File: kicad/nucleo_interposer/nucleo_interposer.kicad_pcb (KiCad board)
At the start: 2 copper layers, 20.3 x 52.3 mm, 5 parts, among them J1 Conn_02x08_Odd_Even, U1 NUCLEO-F303K8-HEADER

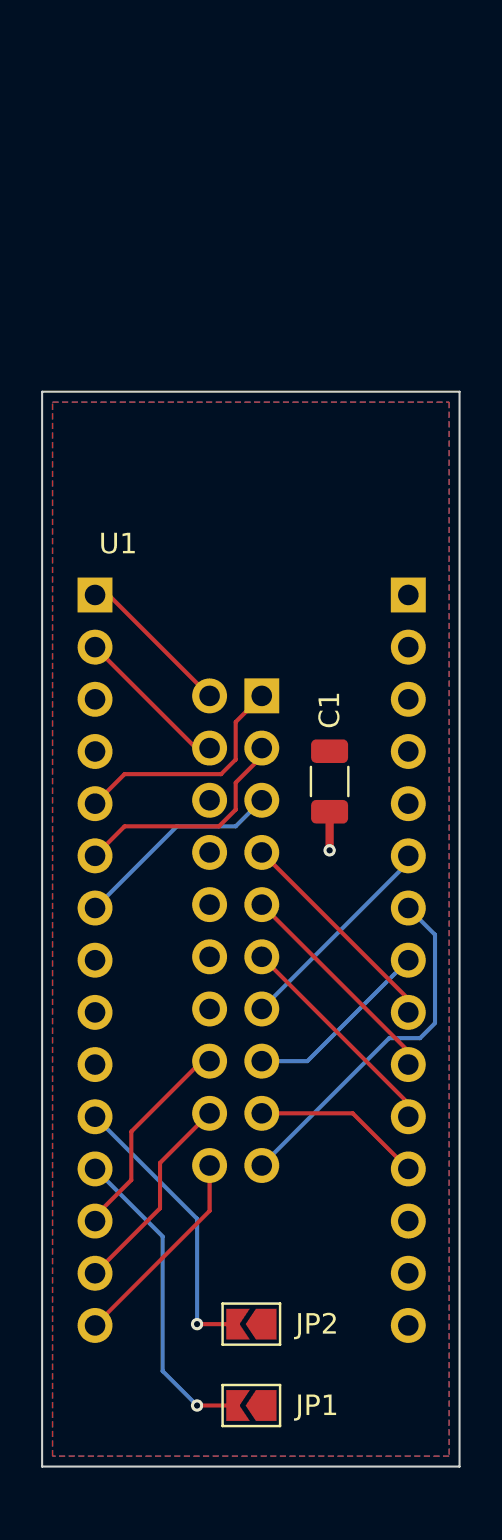
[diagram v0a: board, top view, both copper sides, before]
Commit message: add nucleo interposer step and make it smaller
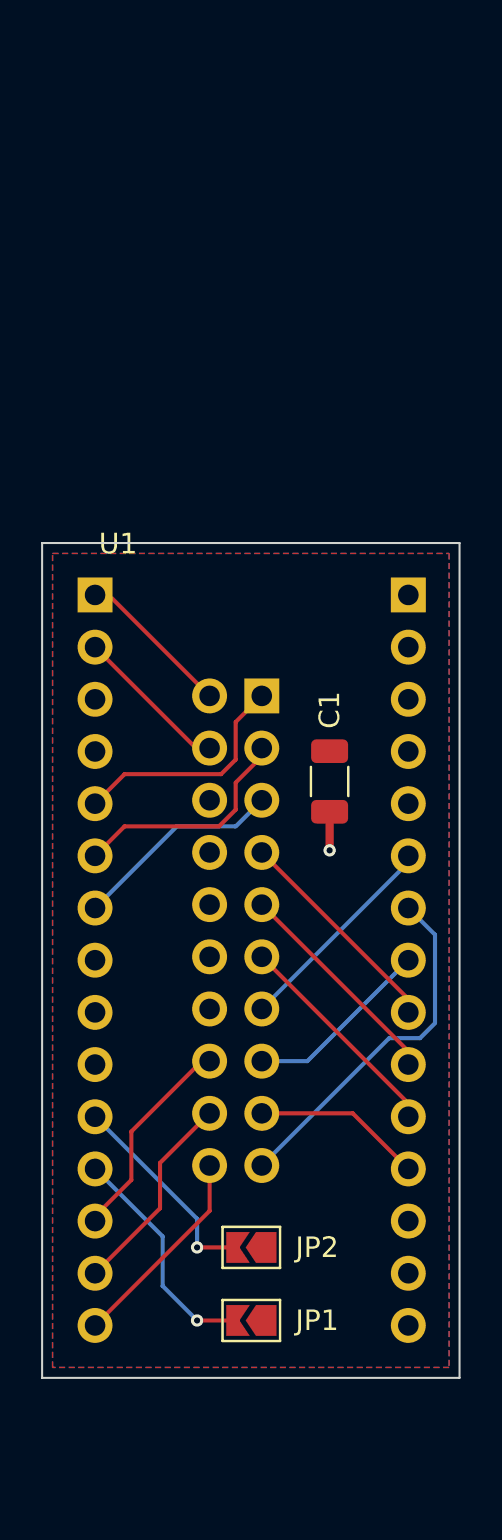
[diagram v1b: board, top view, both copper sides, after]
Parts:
- moved JP1 4.14 mm to (143.9, 106.3)
- moved JP2 3.73 mm to (143.9, 102.7)
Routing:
- net Net-(U1-PA8): track 15.5 -> 11.4 mm
- net Net-(U1-PF1): track 14.1 -> 10.3 mm
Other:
- board size 20.3 x 52.3 mm -> 20.3 x 40.6 mm
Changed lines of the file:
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@@
     )
     (pad_to_mask_clearance 0)
-    (grid_origin 144.4244 75.8952)
+    (grid_origin 133.731 113.411)
     (pcbplotparams
       (layerselection 0x00010fc_ffffffff)
@@
   (net 30 "unconnected-(U1-PB3)")
   (footprint "Jumper:SolderJumper-2_P1.3mm_Open_TrianglePad1.0x1.5mm" (layer "F.Cu")
-    (at 143.9164 110.4392 180)
+    (at 143.9164 106.299 180)
     (descr "SMD Solder Jumper, 1x1.5mm Triangular Pads, 0.3mm gap, open")
     (tags "solder jumper open")
@@
   )
   (footprint "Jumper:SolderJumper-2_P1.3mm_Open_TrianglePad1.0x1.5mm" (layer "F.Cu")
-    (at 143.9164 106.4768 180)
+    (at 143.9164 102.743 180)
     (descr "SMD Solder Jumper, 1x1.5mm Triangular Pads, 0.3mm gap, open")
     (tags "solder jumper open")
@@
     )
   )
-  (gr_rect (start 133.731 61.087) (end 154.051 113.411)
+  (gr_rect (start 133.731 68.453) (end 154.051 109.093)
     (stroke (width 0.1) (type default)) (fill none) (layer "Edge.Cuts"))
   (segment (start 147.7264 81.5358) (end 147.7264 83.4136) (width 0.4) (layer "F.Cu") (net 1))
@@
   (segment (start 141.8844 100.9646) (end 141.8844 98.7552) (width 0.2) (layer "F.Cu") (net 18))
   (segment (start 136.308 106.541) (end 141.8844 100.9646) (width 0.2) (layer "F.Cu") (net 18))
-  (segment (start 143.1914 110.4392) (end 141.2748 110.4392) (width 0.2) (layer "F.Cu") (net 19))
-  (via (at 141.2748 110.4392) (size 0.6) (drill 0.3) (layers "F.Cu" "B.Cu") (net 19))
+  (segment (start 143.1914 106.299) (end 141.2748 106.299) (width 0.2) (layer "F.Cu") (net 19))
+  (via (at 141.2748 106.299) (size 0.6) (drill 0.3) (layers "F.Cu" "B.Cu") (net 19))
   (segment (start 139.5984 102.2114) (end 136.308 98.921) (width 0.2) (layer "B.Cu") (net 19))
-  (segment (start 139.5984 108.7628) (end 139.5984 102.2114) (width 0.2) (layer "B.Cu") (net 19))
-  (segment (start 141.2748 110.4392) (end 139.5984 108.7628) (width 0.2) (layer "B.Cu") (net 19))
-  (segment (start 143.1914 106.4768) (end 141.2748 106.4768) (width 0.2) (layer "F.Cu") (net 20))
-  (via (at 141.2748 106.4768) (size 0.6) (drill 0.3) (layers "F.Cu" "B.Cu") (net 20))
+  (segment (start 141.2748 106.299) (end 139.5984 104.6226) (width 0.2) (layer "B.Cu") (net 19))
+  (segment (start 139.5984 104.6226) (end 139.5984 102.2114) (width 0.2) (layer "B.Cu") (net 19))
+  (segment (start 143.1914 102.743) (end 141.2748 102.743) (width 0.2) (layer "F.Cu") (net 20))
+  (via (at 141.2748 102.743) (size 0.6) (drill 0.3) (layers "F.Cu" "B.Cu") (net 20))
   (segment (start 141.2748 101.3478) (end 136.308 96.381) (width 0.2) (layer "B.Cu") (net 20))
-  (segment (start 141.2748 106.4768) (end 141.2748 101.3478) (width 0.2) (layer "B.Cu") (net 20))
+  (segment (start 141.2748 101.3478) (end 141.2748 102.743) (width 0.2) (layer "B.Cu") (net 20))
   (zone (net 2) (net_name "+5V") (layer "F.Cu") (hatch edge 0.508)
     (connect_pads (clearance 0.254))
@@
     (polygon
       (pts
-        (xy 153.543 112.903)
-        (xy 134.239 112.903)
-        (xy 134.239 61.595)
-        (xy 153.543 61.595)
+        (xy 153.543 108.585)
+        (xy 134.239 108.585)
+        (xy 134.239 68.961)
+        (xy 153.543 68.961)
       )
     )
@@
     (polygon
       (pts
-        (xy 153.543 112.903)
-        (xy 134.239 112.903)
-        (xy 134.239 61.595)
-        (xy 153.543 61.595)
+        (xy 153.543 108.585)
+        (xy 134.239 108.585)
+        (xy 134.239 68.961)
+        (xy 153.543 68.961)
       )
     )

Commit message: move JPS and cap to back
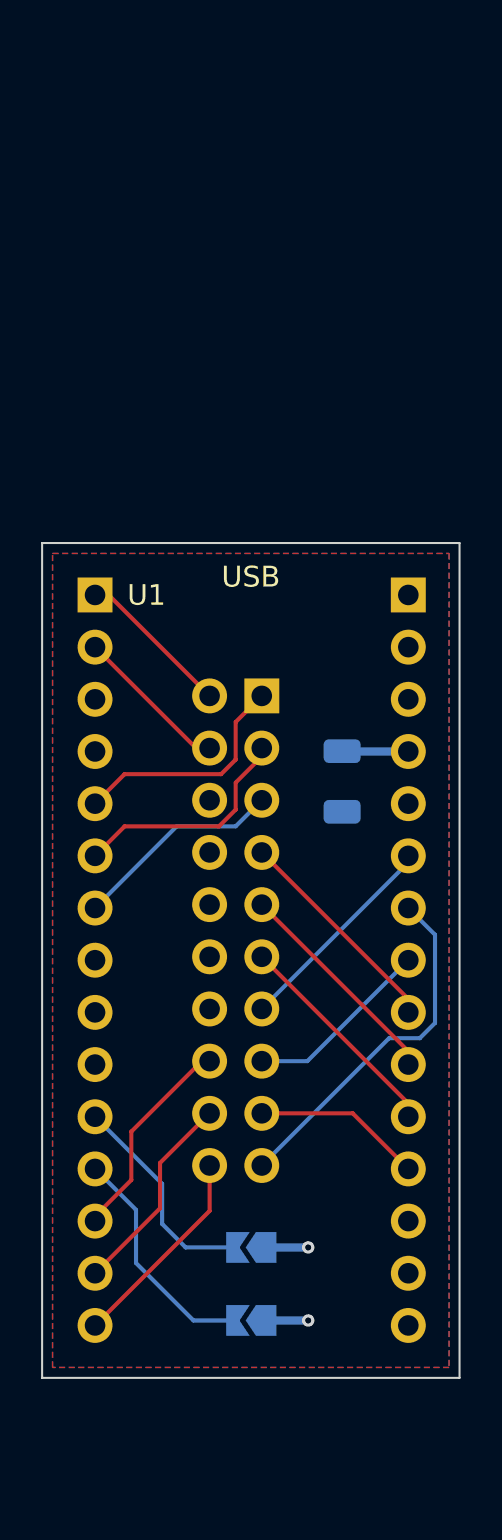
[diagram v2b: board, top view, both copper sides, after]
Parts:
- C1, JP1, JP2: moved to B.Cu
- moved C1 0.61 mm to (148.3, 80.1)
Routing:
- net +5V: track 0.00 -> 7.34 mm, vias 0 -> 2
- net GND: track 1.88 -> 0.00 mm, vias 1 -> 0
- net Net-(U1-PF1): track 10.3 -> 10.7 mm, vias 1 -> 0
- net Net-(U1-PA8): track 11.4 -> 11.5 mm, vias 1 -> 0
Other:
- board text added: "USB"

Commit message: add mounts for nucleo interposer
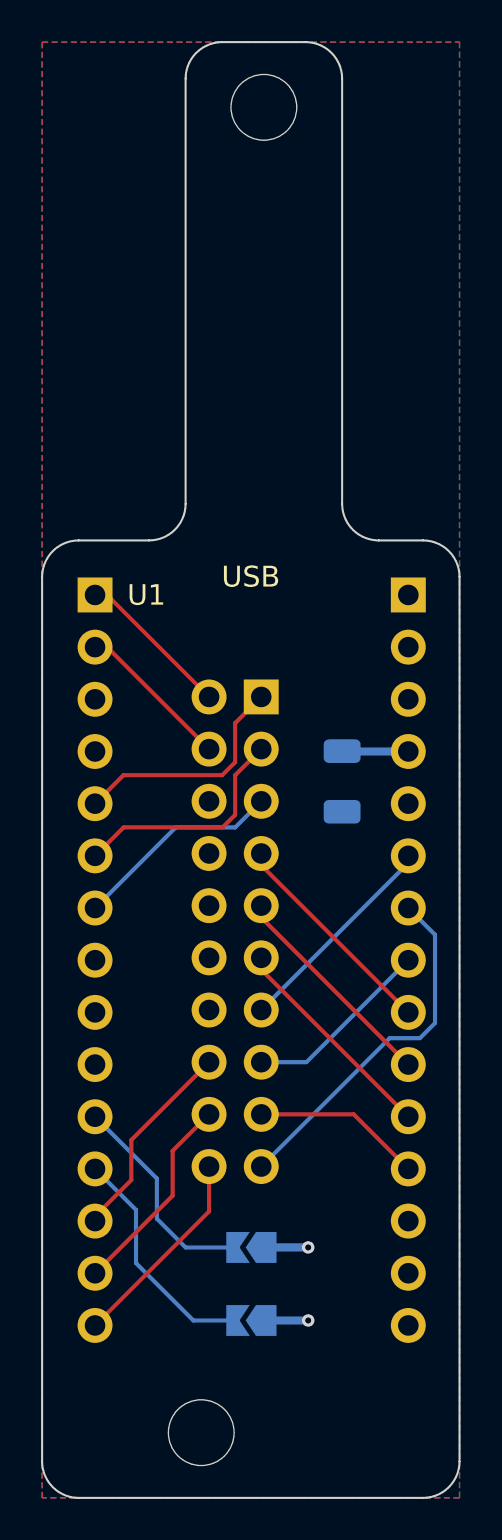
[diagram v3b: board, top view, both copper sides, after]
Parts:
- added REF**: MountingHole_3.2mm_M3, MountingHole:MountingHole_3.2mm_M3, F.Cu at (141.5, 111.8)
- added REF**: MountingHole_3.2mm_M3, MountingHole:MountingHole_3.2mm_M3, F.Cu at (144.5, 47.2)
- moved J1 0.06 mm to (144.4, 75.9)
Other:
- board size 20.3 x 40.6 mm -> 20.3 x 70.9 mm

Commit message: update pcb
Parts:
- removed REF** (x2): MountingHole_3.2mm_M3, MountingHole:MountingHole_3.2mm_M3
- added H1: MountingHole, mio:MountingHole_3.2mm_M3, F.Cu at (144.5, 47.2)
- added H2: MountingHole, mio:MountingHole_3.2mm_M3, F.Cu at (141.5, 111.8)
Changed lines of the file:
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@@
   (net 17 "/SPI1_MISO")
   (net 18 "/NCV_EN_4")
-  (net 19 "Net-(U1-PA8)")
-  (net 20 "Net-(U1-PF1)")
+  (net 19 "Net-(JP1-B)")
+  (net 20 "Net-(JP2-B)")
   (net 21 "unconnected-(U1-NRST)")
   (net 22 "unconnected-(U1-PB6)")
@@
   (net 29 "unconnected-(U1-+3V3)")
   (net 30 "unconnected-(U1-PB3)")
-  (footprint "MountingHole:MountingHole_3.2mm_M3" (layer "F.Cu")
+  (footprint "mio:MountingHole_3.2mm_M3" (layer "F.Cu")
     (at 141.478 111.76)
     (descr "Mounting Hole 3.2mm, no annular, M3")
     (tags "mounting hole 3.2mm no annular m3")
-    (attr exclude_from_pos_files exclude_from_bom)
-    (fp_text reference "REF**" (at 0 -4.2) (layer "F.SilkS") hide
-        (effects (font (size 1 1) (thickness 0.15)))
-    )
-    (fp_text value "MountingHole_3.2mm_M3" (at 0 4.2) (layer "F.Fab")
+    (property "Sheetfile" "nucleo_interposer.kicad_sch")
+    (property "Sheetname" "")
+    (clearance 1.524)
+    (attr exclude_from_pos_files)
+    (fp_text reference "H2" (at 0 -4.2) (layer "F.SilkS") hide
+        (effects (font (size 1 1) (thickness 0.15)))
+    )
+    (fp_text value "MountingHole" (at 0 4.2) (layer "F.Fab")
         (effects (font (size 1 1) (thickness 0.15)))
     )
@@
       (stroke (width 0.05) (type solid)) (fill none) (layer "F.CrtYd"))
     (pad "" np_thru_hole circle (at 0 0) (size 3.2 3.2) (drill 3.2) (layers *.Cu *.Mask))
+    (model "/home/spetroce/code/src/lgl3/kicad/parts/91239A111_M3_6.STEP"
+      (offset (xyz 0 0 -2.159))
+      (scale (xyz 1 1 1))
+      (rotate (xyz 0 0 0))
+    )
   )
   (footprint "mio:NUCLEO-F303K8-HEADER" (layer "F.Cu")
@@
       (net 24 "unconnected-(U1-PF0)") (pinfunction "PF0") (pintype "no_connect"))
     (pad "11" thru_hole circle (at 1.675 -16.2) (size 1.7 1.7) (drill 1) (layers *.Cu *.Mask)
-      (net 20 "Net-(U1-PF1)") (pinfunction "PF1") (pintype "bidirectional"))
+      (net 20 "Net-(JP2-B)") (pinfunction "PF1") (pintype "bidirectional"))
     (pad "12" thru_hole circle (at 1.675 -13.66) (size 1.7 1.7) (drill 1) (layers *.Cu *.Mask)
-      (net 19 "Net-(U1-PA8)") (pinfunction "PA8") (pintype "bidirectional"))
+      (net 19 "Net-(JP1-B)") (pinfunction "PA8") (pintype "bidirectional"))
     (pad "13" thru_hole circle (at 1.675 -11.12) (size 1.7 1.7) (drill 1) (layers *.Cu *.Mask)
       (net 14 "/NCV_EN_2") (pinfunction "PA11") (pintype "bidirectional"))
@@
     )
   )
-  (footprint "MountingHole:MountingHole_3.2mm_M3" (layer "F.Cu")
+  (footprint "mio:MountingHole_3.2mm_M3" (layer "F.Cu")
     (at 144.526 47.244)
     (descr "Mounting Hole 3.2mm, no annular, M3")
     (tags "mounting hole 3.2mm no annular m3")
-    (attr exclude_from_pos_files exclude_from_bom)
-    (fp_text reference "REF**" (at 0 -4.2) (layer "F.SilkS") hide
-        (effects (font (size 1 1) (thickness 0.15)))
-    )
-    (fp_text value "MountingHole_3.2mm_M3" (at 0 4.2) (layer "F.Fab")
+    (property "Sheetfile" "nucleo_interposer.kicad_sch")
+    (property "Sheetname" "")
+    (clearance 1.524)
+    (attr exclude_from_pos_files)
+    (fp_text reference "H1" (at 0 -4.2) (layer "F.SilkS") hide
+        (effects (font (size 1 1) (thickness 0.15)))
+    )
+    (fp_text value "MountingHole" (at 0 4.2) (layer "F.Fab")
         (effects (font (size 1 1) (thickness 0.15)))
     )
@@
       (stroke (width 0.05) (type solid)) (fill none) (layer "F.CrtYd"))
     (pad "" np_thru_hole circle (at 0 0) (size 3.2 3.2) (drill 3.2) (layers *.Cu *.Mask))
+    (model "/home/spetroce/code/src/lgl3/kicad/parts/91239A111_M3_6.STEP"
+      (offset (xyz 0 0 -2.159))
+      (scale (xyz 1 1 1))
+      (rotate (xyz 0 0 0))
+    )
   )
   (footprint "Connector_PinHeader_2.54mm:PinHeader_2x10_P2.54mm_Vertical" (layer "B.Cu")
@@
       ))
     (pad "2" smd custom (at 0.725 0 180) (size 0.3 0.3) (layers "B.Cu" "B.Mask")
-      (net 19 "Net-(U1-PA8)") (pinfunction "B") (pintype "passive") (zone_connect 2) (thermal_bridge_angle 45)
+      (net 19 "Net-(JP1-B)") (pinfunction "B") (pintype "passive") (zone_connect 2) (thermal_bridge_angle 45)
       (options (clearance outline) (anchor rect))
       (primitives
@@
       ))
     (pad "2" smd custom (at 0.725 0 180) (size 0.3 0.3) (layers "B.Cu" "B.Mask")
-      (net 20 "Net-(U1-PF1)") (pinfunction "B") (pintype "passive") (zone_connect 2) (thermal_bridge_angle 45)
+      (net 20 "Net-(JP2-B)") (pinfunction "B") (pintype "passive") (zone_connect 2) (thermal_bridge_angle 45)
       (options (clearance outline) (anchor rect))
       (primitives

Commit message: dfm
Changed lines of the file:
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@@
-(kicad_pcb (version 20220211) (generator pcbnew)
+(kicad_pcb (version 20220308) (generator pcbnew)
   (general
     (thickness 1.6)
@@
       (layerselection 0x00010fc_ffffffff)
       (disableapertmacros false)
-      (usegerberextensions false)
-      (usegerberattributes true)
-      (usegerberadvancedattributes true)
-      (creategerberjobfile true)
+      (usegerberextensions true)
+      (usegerberattributes false)
+      (usegerberadvancedattributes false)
+      (creategerberjobfile false)
       (dashed_line_dash_ratio 12.000000)
       (dashed_line_gap_ratio 3.000000)
@@
       (psa4output false)
       (plotreference true)
-      (plotvalue true)
+      (plotvalue false)
       (plotinvisibletext false)
       (sketchpadsonfab false)
-      (subtractmaskfromsilk false)
+      (subtractmaskfromsilk true)
       (outputformat 1)
       (mirror false)
-      (drillshape 1)
+      (drillshape 0)
       (scaleselection 1)
-      (outputdirectory "")
+      (outputdirectory "gerber/")
     )
   )
@@
     (property "Sheetfile" "nucleo_interposer.kicad_sch")
     (property "Sheetname" "")
-    (clearance 1.524)
+    (clearance 0.508)
     (attr exclude_from_pos_files)
     (fp_text reference "H2" (at 0 -4.2) (layer "F.SilkS") hide
@@
       (stroke (width 0.05) (type solid)) (fill none) (layer "F.CrtYd"))
     (pad "" np_thru_hole circle (at 0 0) (size 3.2 3.2) (drill 3.2) (layers *.Cu *.Mask))
-    (model "/home/spetroce/code/src/lgl3/kicad/parts/91239A111_M3_6.STEP"
-      (offset (xyz 0 0 -2.159))
-      (scale (xyz 1 1 1))
-      (rotate (xyz 0 0 0))
-    )
   )
   (footprint "mio:NUCLEO-F303K8-HEADER" (layer "F.Cu")
@@
     (property "Sheetfile" "nucleo_interposer.kicad_sch")
     (property "Sheetname" "")
-    (clearance 1.524)
+    (clearance 0.508)
     (attr exclude_from_pos_files)
     (fp_text reference "H1" (at 0 -4.2) (layer "F.SilkS") hide
@@
       (stroke (width 0.05) (type solid)) (fill none) (layer "F.CrtYd"))
     (pad "" np_thru_hole circle (at 0 0) (size 3.2 3.2) (drill 3.2) (layers *.Cu *.Mask))
-    (model "/home/spetroce/code/src/lgl3/kicad/parts/91239A111_M3_6.STEP"
-      (offset (xyz 0 0 -2.159))
-      (scale (xyz 1 1 1))
-      (rotate (xyz 0 0 0))
-    )
   )
   (footprint "Connector_PinHeader_2.54mm:PinHeader_2x10_P2.54mm_Vertical" (layer "B.Cu")
@@
     (fp_line (start 1.6 0.8) (end 1.6 -0.8)
       (stroke (width 0.1) (type solid)) (layer "B.Fab"))
-    (pad "1" smd roundrect (at -1.475 0 90) (size 1.15 1.8) (layers "B.Cu" "B.Paste" "B.Mask") (roundrect_rratio 0.217391)
+    (pad "1" smd roundrect (at -1.475 0 90) (size 1.15 1.8) (layers "B.Cu" "B.Paste" "B.Mask") (roundrect_rratio 0.2173913043)
       (net 1 "GND") (pintype "passive"))
-    (pad "2" smd roundrect (at 1.475 0 90) (size 1.15 1.8) (layers "B.Cu" "B.Paste" "B.Mask") (roundrect_rratio 0.217391)
+    (pad "2" smd roundrect (at 1.475 0 90) (size 1.15 1.8) (layers "B.Cu" "B.Paste" "B.Mask") (roundrect_rratio 0.2173913043)
       (net 2 "+5V") (pintype "passive"))
     (model "${KICAD6_3DMODEL_DIR}/Capacitor_SMD.3dshapes/C_1206_3216Metric.wrl"
